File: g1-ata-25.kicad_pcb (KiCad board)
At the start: 2 copper layers, 81.3 x 130.4 mm, 40 parts, among them P1 G1_DC_SOCKET, P2 G1_GD_PLUGNH, P3 IDE_40PIN, P4 IDE_44PIN, P5 CONN_01X02, P6 CONN_01X04, P7 CONN_01X04, P8 CONN_01X05, U1 DSC1001, U2 TS30011-M050

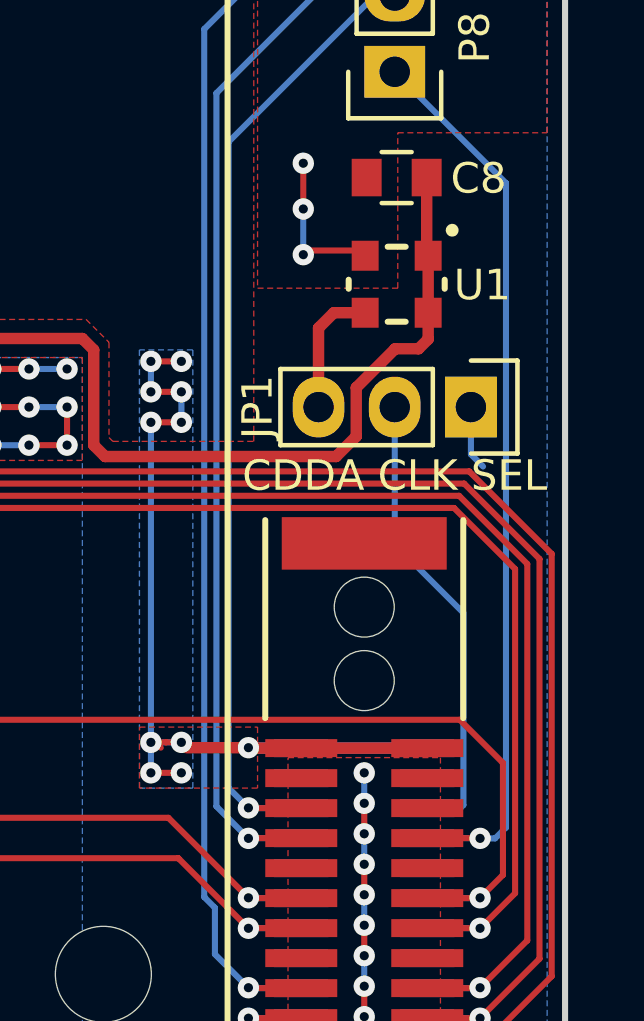
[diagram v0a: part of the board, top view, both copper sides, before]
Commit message: Fixed connection to pass CDDA_CLK from GD-ROM drive.
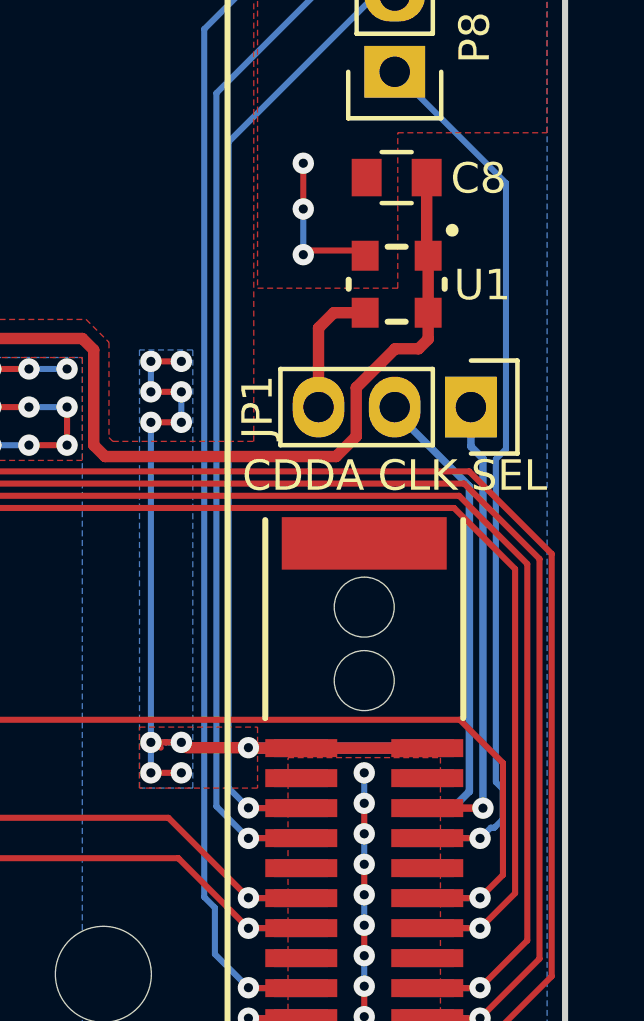
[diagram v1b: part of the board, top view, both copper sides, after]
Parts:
- C5: value C -> 22n
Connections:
- JP1 pad 1: GND -> Net-(JP1-Pad1)
- P1 pad B23: Net-(P1-PadB23) -> Net-(JP1-Pad1)
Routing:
- net Net-(JP1-Pad1): track 0.00 -> 15.4 mm, vias 0 -> 1
- net GND: track 77.7 -> 75.6 mm
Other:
- net class Default: trace_width 0.2032 -> 0.25
